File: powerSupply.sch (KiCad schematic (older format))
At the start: 13 parts, among them J10 Bat_Bak_Byp_Gnd, J11 USB_B_Micro_OUT, J12 ON_Switch, J18 Bat_Bak_Byp_Vcc, J8 Supply_Safety_Bypass, J9 USB_B_Micro_IN, Q1 Q_PMOS_GSD, Q2 FDC021N30, U3 TPS2400BVR

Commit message: Changed USB footprints and did some more routing
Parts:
- J11, J9: footprint Connector_USB:USB_Micro-B_GCT_USB3076-30-A -> Connector_USB:USB_Micro-B
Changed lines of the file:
@@
 F 0 "J11" H 8155 3117 50  0000 C CNN
 F 1 "USB_B_Micro_OUT" H 8155 3026 50  0000 C CNN
-F 2 "Connector_USB:USB_Micro-B_GCT_USB3076-30-A" H 8250 2600 50  0001 C CNN
+F 2 "Connector_USB:USB_Micro-B" H 8250 2600 50  0001 C CNN
 F 3 "~" H 8250 2600 50  0001 C CNN
 	1    8100 2650
@@
 F 0 "J9" H 7155 3117 50  0000 C CNN
 F 1 "USB_B_Micro_IN" H 7155 3026 50  0000 C CNN
-F 2 "Connector_USB:USB_Micro-B_GCT_USB3076-30-A" H 7250 2600 50  0001 C CNN
+F 2 "Connector_USB:USB_Micro-B" H 7250 2600 50  0001 C CNN
 F 3 "~" H 7250 2600 50  0001 C CNN
 	1    7100 2650

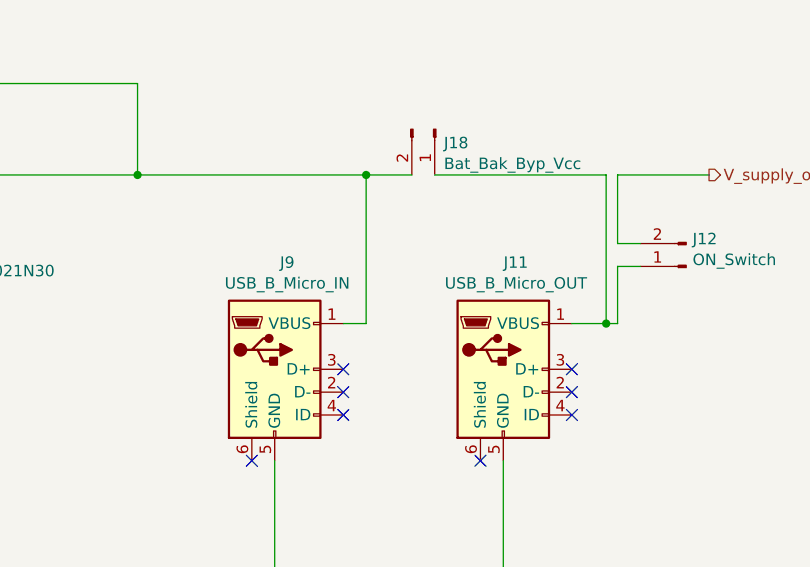
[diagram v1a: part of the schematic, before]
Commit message: Some more routing done. Only 3-4 nets remaining to be routed
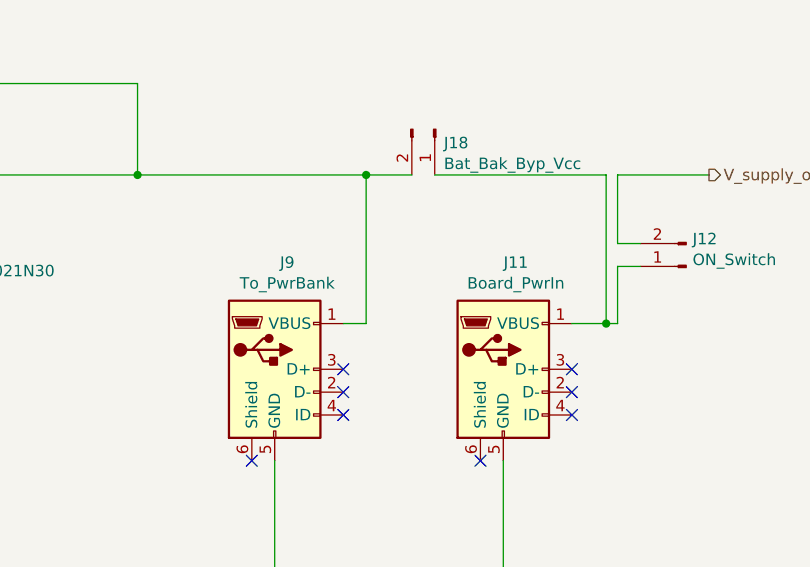
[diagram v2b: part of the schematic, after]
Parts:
- J11: value USB_B_Micro_OUT -> Board_PwrIn
- J9: value USB_B_Micro_IN -> To_PwrBank
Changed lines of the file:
@@
 P 8100 2650
 F 0 "J11" H 8155 3117 50  0000 C CNN
-F 1 "USB_B_Micro_OUT" H 8155 3026 50  0000 C CNN
+F 1 "Board_PwrIn" H 8155 3026 50  0000 C CNN
 F 2 "Connector_USB:USB_Micro-B" H 8250 2600 50  0001 C CNN
 F 3 "~" H 8250 2600 50  0001 C CNN
@@
 P 7100 2650
 F 0 "J9" H 7155 3117 50  0000 C CNN
-F 1 "USB_B_Micro_IN" H 7155 3026 50  0000 C CNN
+F 1 "To_PwrBank" H 7155 3026 50  0000 C CNN
 F 2 "Connector_USB:USB_Micro-B" H 7250 2600 50  0001 C CNN
 F 3 "~" H 7250 2600 50  0001 C CNN

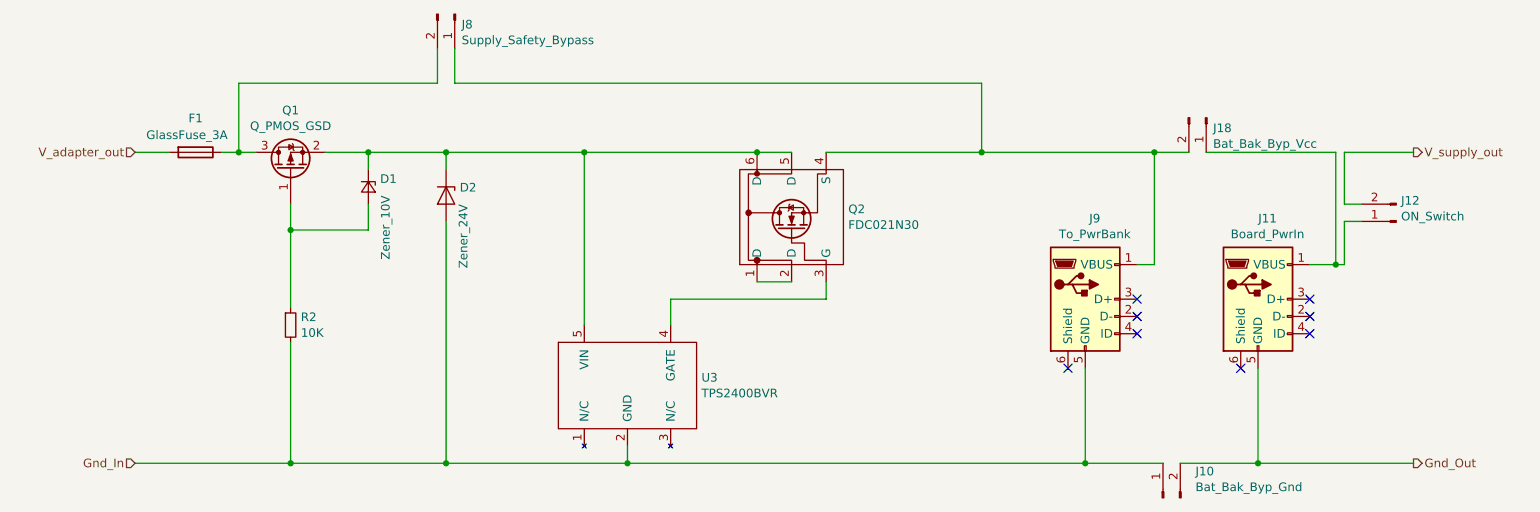
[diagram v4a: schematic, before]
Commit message: Added some more labels to schematics
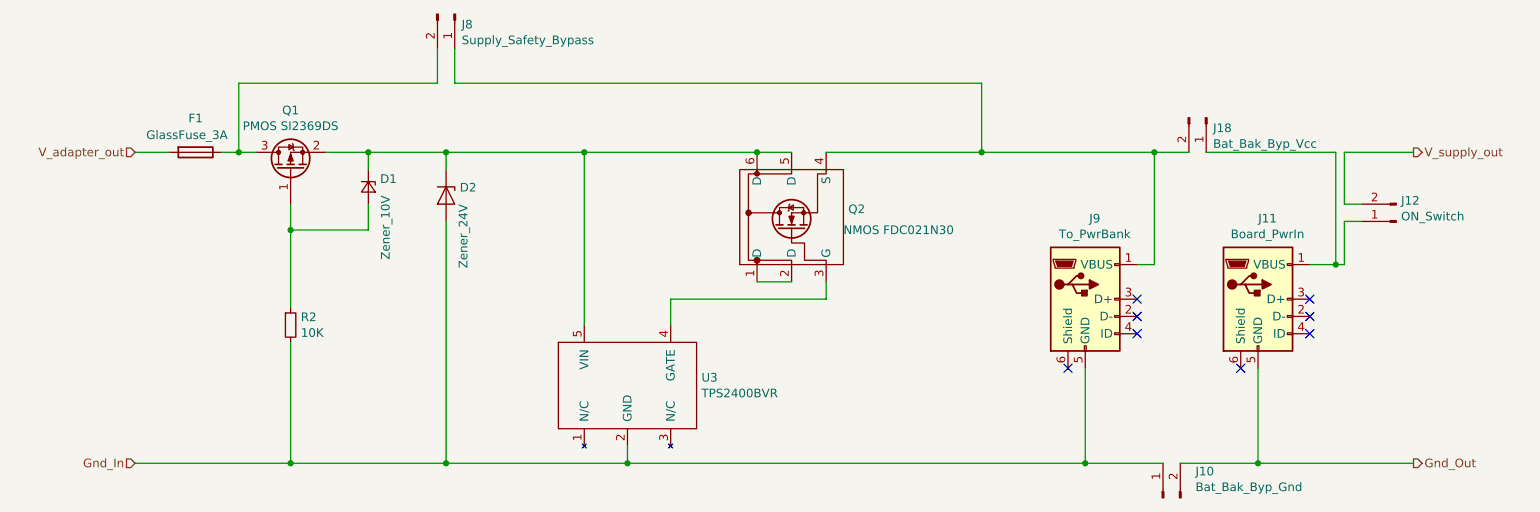
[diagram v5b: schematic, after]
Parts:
- Q1: value Q_PMOS_GSD -> PMOS SI2369DS
- Q2: value FDC021N30 -> NMOS FDC021N30
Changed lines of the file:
@@
 P 2500 1900
 F 0 "Q1" V 2843 1900 50  0000 C CNN
-F 1 "Q_PMOS_GSD" V 2752 1900 50  0000 C CNN
+F 1 "PMOS SI2369DS" V 2752 1900 50  0000 C CNN
 F 2 "Package_TO_SOT_SMD:SOT-23" H 2700 2000 50  0001 C CNN
 F 3 "~" H 2500 1900 50  0001 C CNN
@@
 P 5400 2150
 F 0 "Q2" V 5421 1822 50  0000 R CNN
-F 1 "FDC021N30" V 5330 1822 50  0000 R CNN
+F 1 " NMOS FDC021N30" V 5300 1850 50  0000 R CNN
 F 2 "Package_TO_SOT_SMD:SuperSOT-6" H 5400 1850 50  0001 C CNN
 F 3 "https://www.mouser.in/datasheet/2/308/FDC021N30-1119132.pdf" H 5400 1850 50  0001 C CNN
